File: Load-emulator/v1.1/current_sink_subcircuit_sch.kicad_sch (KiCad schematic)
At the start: 3 parts, among them Q13 TIP41C, U2 LM318H

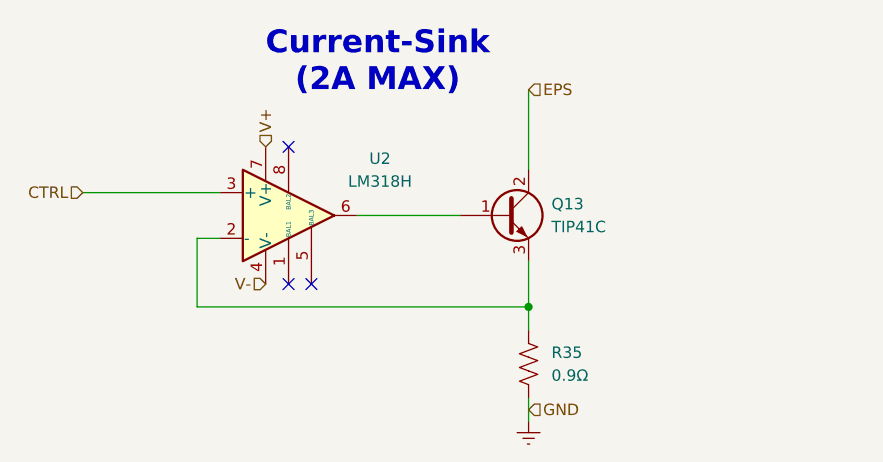
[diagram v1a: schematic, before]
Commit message: Foram adicionados todos os canais, removidos os pinos de conexao para o REPS, foram feitas todas as trilhas de potência, controle e alimentação, com exceção do GND.
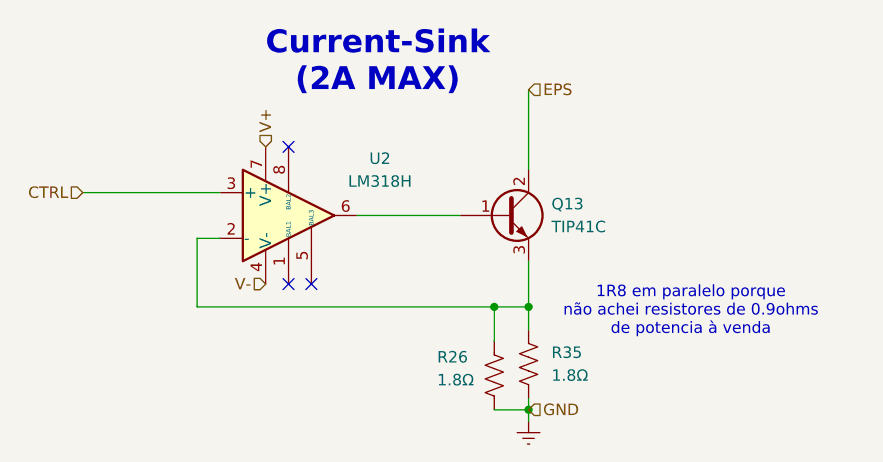
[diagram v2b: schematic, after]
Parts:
- added R26: 1.8Ω, Resistor_SMD:R_0201_0603Metric, symbol Device:R_US
- R35: value 0.9Ω -> 1.8Ω
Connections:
- net Earth: now also R26.2
- net at Q13.3 (E), R35.1, U2.2 (-): now also R26.1
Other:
- note added: "1R8 em paralelo porque não achei resistores de 0.9ohms de potencia à venda"
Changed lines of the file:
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@@
 		)
+	)
+	(text "1R8 em paralelo porque\nnão achei resistores de 0.9ohms\nde potencia à venda"
+		(exclude_from_sim no)
+		(at 183.134 100.838 0)
+		(effects
+			(font
+				(size 1.27 1.27)
+			)
+		)
+	)
+	(junction
+		(at 165.1 111.76)
+		(diameter 0)
+		(color 0 0 0 0)
 	)
 	(junction
@@
 		(color 0 0 0 0)
 	)
+	(junction
+		(at 161.29 100.33)
+		(diameter 0)
+		(color 0 0 0 0)
+	)
 	(no_connect
 		(at 138.43 97.79)
@@
 	(wire
 		(pts
+			(xy 161.29 111.76) (xy 165.1 111.76)
+		)
+		(stroke
+			(width 0)
+			(type default)
+		)
+	)
+	(wire
+		(pts
 			(xy 165.1 76.2) (xy 165.1 85.09)
 		)
@@
 	(wire
 		(pts
-			(xy 165.1 110.49) (xy 165.1 113.03)
-		)
-		(stroke
-			(width 0)
-			(type default)
-		)
-	)
-	(wire
-		(pts
-			(xy 128.27 100.33) (xy 165.1 100.33)
+			(xy 161.29 100.33) (xy 161.29 104.14)
+		)
+		(stroke
+			(width 0)
+			(type default)
+		)
+	)
+	(wire
+		(pts
+			(xy 165.1 110.49) (xy 165.1 111.76)
+		)
+		(stroke
+			(width 0)
+			(type default)
+		)
+	)
+	(wire
+		(pts
+			(xy 128.27 100.33) (xy 161.29 100.33)
 		)
 		(stroke
@@
 	(wire
 		(pts
+			(xy 161.29 100.33) (xy 165.1 100.33)
+		)
+		(stroke
+			(width 0)
+			(type default)
+		)
+	)
+	(wire
+		(pts
 			(xy 128.27 92.71) (xy 130.81 92.71)
 		)
@@
 		(pts
 			(xy 115.57 87.63) (xy 130.81 87.63)
+		)
+		(stroke
+			(width 0)
+			(type default)
+		)
+	)
+	(wire
+		(pts
+			(xy 165.1 111.76) (xy 165.1 113.03)
 		)
 		(stroke
@@
 			)
 		)
-		(property "Value" "0.9Ω"
+		(property "Value" "1.8Ω"
 			(at 167.64 107.9499 0)
 			(effects
@@
 					(unit 1)
 				)
+			)
+		)
+	)
+	(symbol
+		(lib_id "Device:R_US")
+		(at 161.29 107.95 0)
+		(unit 1)
+		(exclude_from_sim no)
+		(in_bom yes)
+		(on_board yes)
+		(dnp no)
+		(property "Reference" "R26"
+			(at 154.94 105.918 0)
+			(effects
+				(font
+					(size 1.27 1.27)
+				)
+				(justify left)
+			)
+		)
+		(property "Value" "1.8Ω"
+			(at 154.94 108.458 0)
+			(effects
+				(font
+					(size 1.27 1.27)
+				)
+				(justify left)
+			)
+		)
+		(property "Footprint" "Resistor_SMD:R_0201_0603Metric"
+			(at 162.306 108.204 90)
+			(effects
+				(font
+					(size 1.27 1.27)
+				)
+				(hide yes)
+			)
+		)
+		(property "Datasheet" "~"
+			(at 161.29 107.95 0)
+			(effects
+				(font
+					(size 1.27 1.27)
+				)
+				(hide yes)
+			)
+		)
+		(property "Description" "Resistor, US symbol"
+			(at 161.29 107.95 0)
+			(effects
+				(font
+					(size 1.27 1.27)
+				)
+				(hide yes)
+			)
+		)
+		(pin "1"
+		)
+		(pin "2"
+		)
+		(instances
+			(project "Load-emulator"
+				(path "/9054bfd2-3cc0-4c96-aa71-abdb09b76dc7/a12c045f-372a-4c5b-93d1-0c234b5f9c5c/128c0139-7aee-4d92-8032-2b2c6fcc70a3"
+					(reference "R28.1")
+					(unit 1)
+				)
+				(path "/9054bfd2-3cc0-4c96-aa71-abdb09b76dc7/a12c045f-372a-4c5b-93d1-0c234b5f9c5c/87a0f9ee-fa92-48a0-98d1-72d297c3468c"
+					(reference "R36")
+					(unit 1)
+				)
+				(path "/9054bfd2-3cc0-4c96-aa71-abdb09b76dc7/a12c045f-372a-4c5b-93d1-0c234b5f9c5c/c40377b4-6929-4e4a-ac2d-4b484617f896"
+					(reference "R26")
+					(unit 1)
+				)
+				(path "/9054bfd2-3cc0-4c96-aa71-abdb09b76dc7/a12c045f-372a-4c5b-93d1-0c234b5f9c5c/e0ddf382-1b56-45d3-a566-5cd39e11bb78"
+					(reference "R20.1")
+					(unit 1)
+				)
+				(path "/9054bfd2-3cc0-4c96-aa71-abdb09b76dc7/a12c045f-372a-4c5b-93d1-0c234b5f9c5c/ecd08cfa-ace2-4c26-a75b-4cdb3b0fd9bc"
+					(reference "R37")
+					(unit 1)
+				)

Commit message: Todos erros foram consertados, assim como todos os avisos, com exceção dos que se referem ao PC104, que teve seu footprint modificado. Todos modelos 3D foram corretamente upados. Adição de zonas de GND.
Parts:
- R26, R35: footprint Resistor_SMD:R_0201_0603Metric -> Resistor_THT:R_Axial_DIN0207_L6.3mm_D2.5mm_P2.54mm_Vertical
- U2: footprint LM318M:SOIC127P599X175-8N -> footprints:SOIC127P599X175-8N
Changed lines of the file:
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@@
 			)
 		)
-		(property "Footprint" "Resistor_SMD:R_0201_0603Metric"
+		(property "Footprint" "Resistor_THT:R_Axial_DIN0207_L6.3mm_D2.5mm_P2.54mm_Vertical"
 			(at 166.116 106.934 90)
 			(effects
@@
 			)
 		)
-		(property "Footprint" "LM318M:SOIC127P599X175-8N"
+		(property "Footprint" "footprints:SOIC127P599X175-8N"
 			(at 138.43 90.17 0)
 			(effects
@@
 			)
 		)
-		(property "Footprint" "Resistor_SMD:R_0201_0603Metric"
+		(property "Footprint" "Resistor_THT:R_Axial_DIN0207_L6.3mm_D2.5mm_P2.54mm_Vertical"
 			(at 162.306 108.204 90)
 			(effects
